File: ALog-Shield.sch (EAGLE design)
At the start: 28 parts, among them U1 DS3231MZ/V+T

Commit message: Bobby's caps
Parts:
- added C1, C2, C3, C4: (no value), bschulz_passives:C-EU0.1UFC0603
- CLK_DECOUP: device SparkFun-Passives:CAP0805 -> bschulz_passives:C-EU10UFC0805
- CLOCK_BATT_DECOUP: device rcl:C-EUC0603 -> bschulz_passives:C-EU0.1UFC0603
- R_PU_A, R_PU_L: device resistor:R-US_R0603 -> bschulz_passives:R-EU_10KR0603
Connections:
- net A0: now also C1.1
- net A1: now also C2.1
- net A2: now also C3.1
- net A3: now also C4.1
- net GND: now also C1.2, C2.2, C3.2, C4.2
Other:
- moved on the sheet: CLK_DECOUP
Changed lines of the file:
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@@
 <?xml version="1.0" encoding="utf-8"?>
 <!DOCTYPE eagle SYSTEM "eagle.dtd">
-<eagle version="8.5.0">
+<eagle version="8.6.0">
 <drawing>
 <settings>
@@
 <part name="RESET" library="bschulz" deviceset="BUTTON" device="4.2X3.2" value="Reset"/>
 <part name="SUPPLY53" library="supply2" deviceset="GND" device=""/>
-<part name="CLOCK_BATT_DECOUP" library="rcl" deviceset="C-EU" device="C0603" value="0.1uF"/>
+<part name="CLOCK_BATT_DECOUP" library="bschulz_passives" deviceset="C-EU" device="C0603" technology="0.1UF" value="0.1uF"/>
 <part name="SUPPLY56" library="supply2" deviceset="GND" device=""/>
 <part name="D2" library="semicon-smd-ipc" deviceset="DIODE_AC-CA_" device="" value="BAT54"/>
@@
 <part name="+3V7" library="supply1" deviceset="+3V3" device=""/>
 <part name="U$1" library="awickert" deviceset="NWLOGO_MED" device=""/>
-<part name="CLK_DECOUP" library="SparkFun-Passives" deviceset="CAP" device="0805" value="10 uF"/>
+<part name="CLK_DECOUP" library="bschulz_passives" deviceset="C-EU" device="C0805" technology="10UF" value="10 uF"/>
 <part name="JP1" library="SparkFun-Connectors" deviceset="M02" device="LOCK"/>
 <part name="+3V3" library="supply1" deviceset="+3V3" device=""/>
-<part name="R_PU_L" library="resistor" deviceset="R-US_" device="R0603" value="10k"/>
-<part name="R_PU_A" library="resistor" deviceset="R-US_" device="R0603" value="10k"/>
+<part name="R_PU_L" library="bschulz_passives" deviceset="R-EU_" device="R0603" technology="10K" value="10k"/>
+<part name="R_PU_A" library="bschulz_passives" deviceset="R-EU_" device="R0603" technology="10K" value="10k"/>
+<part name="C1" library="bschulz_passives" deviceset="C-EU" device="C0603" technology="0.1UF"/>
+<part name="C2" library="bschulz_passives" deviceset="C-EU" device="C0603" technology="0.1UF"/>
+<part name="C3" library="bschulz_passives" deviceset="C-EU" device="C0603" technology="0.1UF"/>
+<part name="C4" library="bschulz_passives" deviceset="C-EU" device="C0603" technology="0.1UF"/>
 </parts>
 <sheets>
@@
 <instance part="J3" gate="G$1" x="144.78" y="-137.16" rot="R180"/>
 <instance part="U$1" gate="G$1" x="17.78" y="-27.94"/>
+<instance part="C1" gate="G$1" x="48.26" y="-165.1" rot="R90"/>
+<instance part="C2" gate="G$1" x="48.26" y="-175.26" rot="R90"/>
+<instance part="C3" gate="G$1" x="48.26" y="-185.42" rot="R90"/>
+<instance part="C4" gate="G$1" x="48.26" y="-195.58" rot="R90"/>
 </instances>
 <busses>
@@
 <wire x1="63.5" y1="-185.42" x2="63.5" y2="-195.58" width="0.1524" layer="91"/>
 <wire x1="63.5" y1="-195.58" x2="63.5" y2="-205.74" width="0.1524" layer="91"/>
-<wire x1="63.5" y1="-165.1" x2="50.8" y2="-165.1" width="0.1524" layer="91"/>
-<wire x1="50.8" y1="-175.26" x2="63.5" y2="-175.26" width="0.1524" layer="91"/>
+<wire x1="63.5" y1="-165.1" x2="53.34" y2="-165.1" width="0.1524" layer="91"/>
+<wire x1="53.34" y1="-175.26" x2="63.5" y2="-175.26" width="0.1524" layer="91"/>
 <junction x="63.5" y="-175.26"/>
-<wire x1="50.8" y1="-185.42" x2="63.5" y2="-185.42" width="0.1524" layer="91"/>
+<wire x1="53.34" y1="-185.42" x2="63.5" y2="-185.42" width="0.1524" layer="91"/>
 <junction x="63.5" y="-185.42"/>
-<wire x1="50.8" y1="-195.58" x2="63.5" y2="-195.58" width="0.1524" layer="91"/>
+<wire x1="53.34" y1="-195.58" x2="63.5" y2="-195.58" width="0.1524" layer="91"/>
 <junction x="63.5" y="-195.58"/>
+<pinref part="C1" gate="G$1" pin="2"/>
+<pinref part="C2" gate="G$1" pin="2"/>
+<pinref part="C3" gate="G$1" pin="2"/>
+<pinref part="C4" gate="G$1" pin="2"/>
 </segment>
 <segment>
@@
 <wire x1="35.56" y1="-185.42" x2="45.72" y2="-185.42" width="0.1524" layer="91"/>
 <label x="38.1" y="-185.42" size="1.778" layer="95"/>
+<pinref part="C3" gate="G$1" pin="1"/>
 </segment>
 </net>
@@
 <wire x1="35.56" y1="-165.1" x2="45.72" y2="-165.1" width="0.1524" layer="91"/>
 <label x="38.1" y="-165.1" size="1.778" layer="95"/>
+<pinref part="C1" gate="G$1" pin="1"/>
 </segment>
 </net>
@@
 <wire x1="45.72" y1="-195.58" x2="35.56" y2="-195.58" width="0.1524" layer="91"/>
 <label x="38.1" y="-195.58" size="1.778" layer="95"/>
+<pinref part="C4" gate="G$1" pin="1"/>
 </segment>
 </net>
@@
 <wire x1="35.56" y1="-175.26" x2="45.72" y2="-175.26" width="0.1524" layer="91"/>
 <label x="38.1" y="-175.26" size="1.778" layer="95"/>
+<pinref part="C2" gate="G$1" pin="1"/>
 </segment>
 </net>
@@
 <pinref part="CLOCK_BATT_DECOUP" gate="G$1" pin="2"/>
 <wire x1="99.06" y1="119.38" x2="99.06" y2="124.46" width="0.1524" layer="91"/>
-<wire x1="109.22" y1="124.46" x2="109.22" y2="119.38" width="0.1524" layer="91"/>
+<wire x1="109.22" y1="121.92" x2="109.22" y2="119.38" width="0.1524" layer="91"/>
 <wire x1="109.22" y1="119.38" x2="99.06" y2="119.38" width="0.1524" layer="91"/>
 <wire x1="93.98" y1="129.54" x2="93.98" y2="119.38" width="0.1524" layer="91"/>
@@
 <pinref part="CLOCK_BATT_DECOUP" gate="G$1" pin="1"/>
 <junction x="99.06" y="132.08"/>
-<wire x1="99.06" y1="132.08" x2="109.22" y2="132.08" width="0.1524" layer="91"/>
+<wire x1="99.06" y1="132.08" x2="109.22" y2="129.54" width="0.1524" layer="91"/>
 <pinref part="U1" gate="A" pin="VBAT"/>
-<wire x1="109.22" y1="132.08" x2="137.16" y2="132.08" width="0.1524" layer="91"/>
+<wire x1="109.22" y1="129.54" x2="137.16" y2="132.08" width="0.1524" layer="91"/>
 <wire x1="137.16" y1="132.08" x2="137.16" y2="129.54" width="0.1524" layer="91"/>
 <pinref part="CLOCK_BATT" gate="G$1" pin="+"/>
 <pinref part="CLK_DECOUP" gate="G$1" pin="1"/>
-<junction x="109.22" y="132.08"/>
-</segment>
-</net>
+<junction x="109.22" y="129.54"/>
+</segment>
+</net>

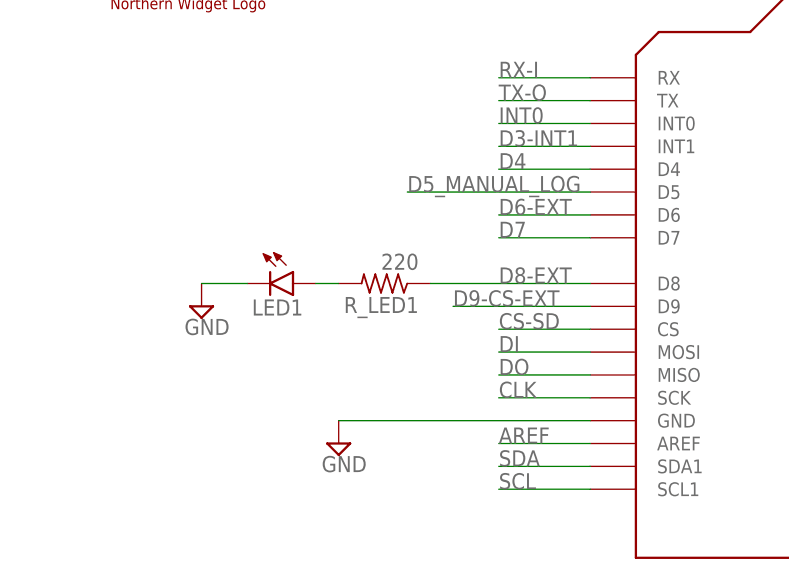
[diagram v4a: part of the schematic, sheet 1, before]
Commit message: R220K to R330K ColdSilicon
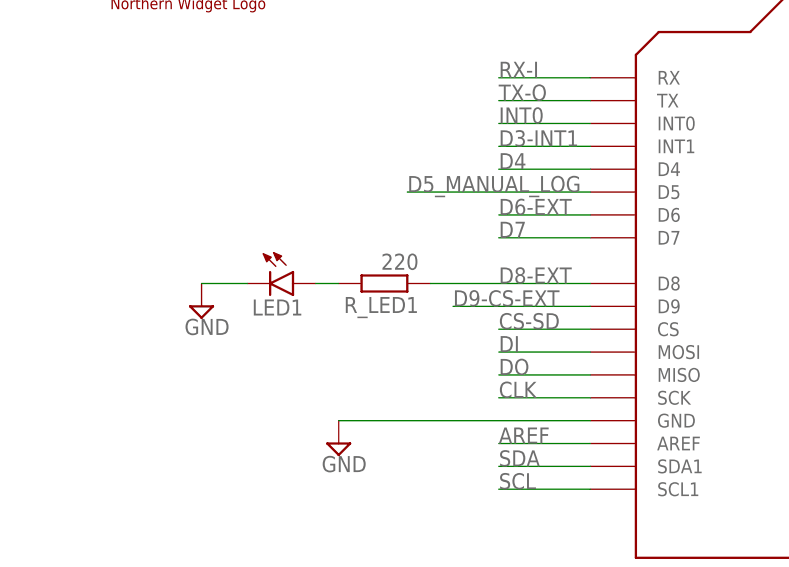
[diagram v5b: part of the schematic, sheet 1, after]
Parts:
- R_LED1: device resistor:R-US_R0603 -> bschulz_passives:R-EU_330R0603
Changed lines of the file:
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@@
 <part name="LED1" library="SparkFun-LED" deviceset="LED" device="1206"/>
 <part name="SUPPLY45" library="supply2" deviceset="GND" device=""/>
-<part name="R_LED1" library="resistor" deviceset="R-US_" device="R0603" value="220"/>
+<part name="R_LED1" library="bschulz_passives" deviceset="R-EU_" device="R0603" technology="330" value="220"/>
 <part name="+3V13" library="supply1" deviceset="+3V3" device=""/>
 <part name="A1" library="resistor" deviceset="R-US_" device="0207/10"/>

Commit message: ColdSilicon DS3231M
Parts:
- removed U1: DS3231MZ/V+T, Maxim-DS3231MZ_8-SOIC:DS3231MZ/V+T
- added RTC1: DS3231M, bschulz:DS3231M
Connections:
- net BAT: now also RTC1.VBAT; no longer U1.VBAT
- net GND: now also RTC1.GND; no longer U1.GND
- net INT0: now also RTC1.SQW; no longer U1.*INT/SQW
- net SCL: now also RTC1.SCL; no longer U1.SCL
- net SDA: now also RTC1.SDA; no longer U1.SDA
- net VCC: now also RTC1.VCC; no longer U1.VCC
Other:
- moved on the sheet: CLK_DECOUP, CLOCK_BATT
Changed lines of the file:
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@@
 <part name="D2" library="semicon-smd-ipc" deviceset="DIODE_AC-CA_" device="" value="BAT54"/>
 <part name="LOG" library="bschulz" deviceset="BUTTON" device="4.2X3.2" value="LOG"/>
-<part name="U1" library="Maxim-DS3231MZ_8-SOIC" deviceset="DS3231MZ/V+T" device=""/>
 <part name="FRAME1" library="frames" deviceset="LETTER_P" device=""/>
 <part name="FRAME3" library="frames" deviceset="LETTER_P" device=""/>
@@
 <part name="C3" library="bschulz_passives" deviceset="C-EU" device="C0603" technology="0.1UF"/>
 <part name="C4" library="bschulz_passives" deviceset="C-EU" device="C0603" technology="0.1UF"/>
+<part name="RTC1" library="bschulz" deviceset="DS3231M" device=""/>
 </parts>
 <sheets>
@@
 <attribute name="VALUE" x="100.584" y="124.841" size="1.778" layer="96"/>
 </instance>
-<instance part="SUPPLY56" gate="GND" x="137.16" y="106.68"/>
-<instance part="U1" gate="A" x="20.32" y="137.16"/>
+<instance part="SUPPLY56" gate="GND" x="137.16" y="91.44"/>
 <instance part="FRAME3" gate="G$1" x="0" y="0"/>
 <instance part="FRAME3" gate="G$2" x="83.82" y="0" smashed="yes">
@@
 <instance part="P+5" gate="VCC" x="124.46" y="152.4"/>
 <instance part="P+7" gate="VCC" x="114.3" y="154.94"/>
-<instance part="P+9" gate="VCC" x="12.7" y="139.7"/>
-<instance part="CLOCK_BATT" gate="G$1" x="137.16" y="121.92" rot="R90"/>
+<instance part="P+9" gate="VCC" x="58.42" y="139.7"/>
+<instance part="CLOCK_BATT" gate="G$1" x="137.16" y="109.22" rot="R90"/>
 <instance part="+3V2" gate="G$1" x="60.96" y="215.9"/>
 <instance part="+3V7" gate="G$1" x="114.3" y="228.6"/>
-<instance part="CLK_DECOUP" gate="G$1" x="109.22" y="127"/>
+<instance part="CLK_DECOUP" gate="G$1" x="109.22" y="129.54"/>
 <instance part="JP1" gate="G$1" x="129.54" y="58.42"/>
 <instance part="+3V3" gate="G$1" x="147.32" y="68.58"/>
 <instance part="R_PU_L" gate="G$1" x="114.3" y="142.24" rot="R270"/>
 <instance part="R_PU_A" gate="G$1" x="124.46" y="139.7" rot="R270"/>
+<instance part="RTC1" gate="G$1" x="78.74" y="132.08"/>
 </instances>
 <busses>
@@
 </segment>
 <segment>
-<wire x1="20.32" y1="134.62" x2="12.7" y2="134.62" width="0.1524" layer="91"/>
-<pinref part="U1" gate="A" pin="VCC"/>
-<wire x1="12.7" y1="134.62" x2="12.7" y2="137.16" width="0.1524" layer="91"/>
+<wire x1="66.04" y1="134.62" x2="58.42" y2="134.62" width="0.1524" layer="91"/>
+<wire x1="58.42" y1="134.62" x2="58.42" y2="137.16" width="0.1524" layer="91"/>
 <pinref part="P+9" gate="VCC" pin="VCC"/>
+<pinref part="RTC1" gate="G$1" pin="VCC"/>
 </segment>
 </net>
@@
 <pinref part="CLOCK_BATT_DECOUP" gate="G$1" pin="2"/>
 <wire x1="99.06" y1="119.38" x2="99.06" y2="124.46" width="0.1524" layer="91"/>
-<wire x1="109.22" y1="121.92" x2="109.22" y2="119.38" width="0.1524" layer="91"/>
+<wire x1="109.22" y1="124.46" x2="109.22" y2="119.38" width="0.1524" layer="91"/>
 <wire x1="109.22" y1="119.38" x2="99.06" y2="119.38" width="0.1524" layer="91"/>
 <wire x1="93.98" y1="129.54" x2="93.98" y2="119.38" width="0.1524" layer="91"/>
@@
 <wire x1="99.06" y1="119.38" x2="93.98" y2="119.38" width="0.1524" layer="91"/>
 <junction x="99.06" y="119.38"/>
-<pinref part="U1" gate="A" pin="GND"/>
 <pinref part="CLK_DECOUP" gate="G$1" pin="2"/>
+<pinref part="RTC1" gate="G$1" pin="GND"/>
 </segment>
 <segment>
 <pinref part="SUPPLY56" gate="GND" pin="GND"/>
-<wire x1="137.16" y1="109.22" x2="137.16" y2="114.3" width="0.1524" layer="91"/>
+<wire x1="137.16" y1="93.98" x2="137.16" y2="101.6" width="0.1524" layer="91"/>
 <pinref part="CLOCK_BATT" gate="G$1" pin="-"/>
 </segment>
@@
 <wire x1="91.44" y1="137.16" x2="114.3" y2="137.16" width="0.1524" layer="91"/>
 <label x="99.06" y="137.16" size="1.778" layer="95"/>
-<pinref part="U1" gate="A" pin="SCL"/>
 <pinref part="R_PU_L" gate="G$1" pin="2"/>
+<pinref part="RTC1" gate="G$1" pin="SCL"/>
 </segment>
 </net>
@@
 <wire x1="91.44" y1="134.62" x2="124.46" y2="134.62" width="0.1524" layer="91"/>
 <label x="99.06" y="134.62" size="1.778" layer="95"/>
-<pinref part="U1" gate="A" pin="SDA"/>
 <pinref part="R_PU_A" gate="G$1" pin="2"/>
+<pinref part="RTC1" gate="G$1" pin="SDA"/>
 </segment>
 </net>
 <net name="INT0" class="0">
 <segment>
-<label x="15.24" y="132.08" size="1.778" layer="95"/>
-<wire x1="20.32" y1="132.08" x2="15.24" y2="132.08" width="0.1524" layer="91"/>
-<pinref part="U1" gate="A" pin="*INT/SQW"/>
+<label x="60.96" y="132.08" size="1.778" layer="95"/>
+<wire x1="66.04" y1="132.08" x2="60.96" y2="132.08" width="0.1524" layer="91"/>
+<pinref part="RTC1" gate="G$1" pin="SQW"/>
 </segment>
 </net>
@@
 <pinref part="CLOCK_BATT_DECOUP" gate="G$1" pin="1"/>
 <junction x="99.06" y="132.08"/>
-<wire x1="99.06" y1="132.08" x2="109.22" y2="129.54" width="0.1524" layer="91"/>
-<pinref part="U1" gate="A" pin="VBAT"/>
-<wire x1="109.22" y1="129.54" x2="137.16" y2="132.08" width="0.1524" layer="91"/>
-<wire x1="137.16" y1="132.08" x2="137.16" y2="129.54" width="0.1524" layer="91"/>
+<wire x1="99.06" y1="132.08" x2="109.22" y2="132.08" width="0.1524" layer="91"/>
+<wire x1="109.22" y1="132.08" x2="137.16" y2="132.08" width="0.1524" layer="91"/>
+<wire x1="137.16" y1="132.08" x2="137.16" y2="116.84" width="0.1524" layer="91"/>
 <pinref part="CLOCK_BATT" gate="G$1" pin="+"/>
 <pinref part="CLK_DECOUP" gate="G$1" pin="1"/>
-<junction x="109.22" y="129.54"/>
-</segment>
-</net>
+<junction x="109.22" y="132.08"/>
+<pinref part="RTC1" gate="G$1" pin="VBAT"/>
+</segment>
+</net>

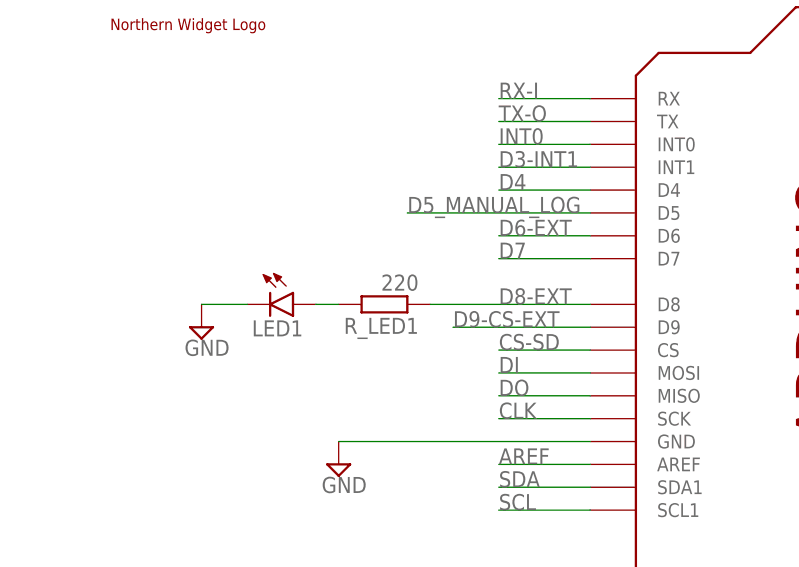
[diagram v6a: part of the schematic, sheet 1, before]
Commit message: R330ohms
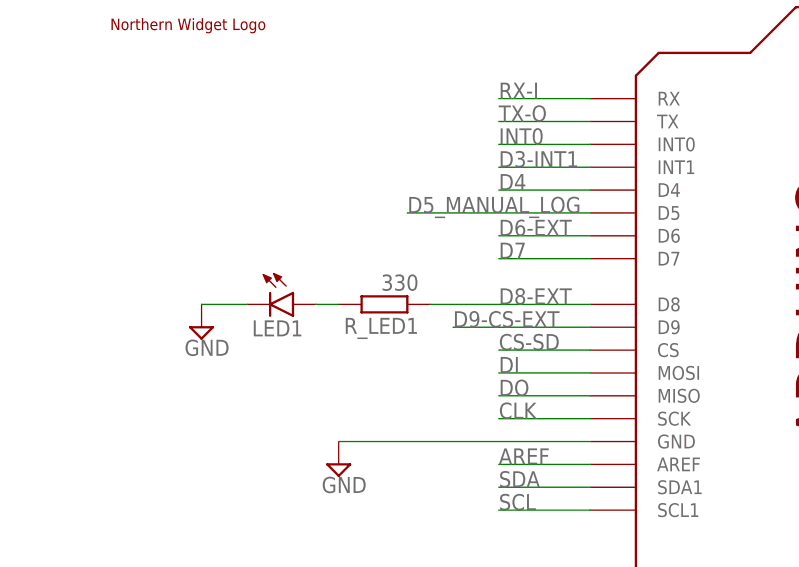
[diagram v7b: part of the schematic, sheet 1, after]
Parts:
- R_LED1: value 220 -> 330
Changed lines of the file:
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@@
 <part name="LED1" library="SparkFun-LED" deviceset="LED" device="1206"/>
 <part name="SUPPLY45" library="supply2" deviceset="GND" device=""/>
-<part name="R_LED1" library="bschulz_passives" deviceset="R-EU_" device="R0603" technology="330" value="220"/>
+<part name="R_LED1" library="bschulz_passives" deviceset="R-EU_" device="R0603" technology="330" value="330"/>
 <part name="+3V13" library="supply1" deviceset="+3V3" device=""/>
 <part name="A1" library="resistor" deviceset="R-US_" device="0207/10"/>
